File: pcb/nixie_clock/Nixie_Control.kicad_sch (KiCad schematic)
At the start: 1 part, among them U13 PCA9685BS

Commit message: nixie pin changes and more wiring
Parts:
- U28: renamed from U13; footprint Package_DFN_QFN:QFN-28-1EP_6x6mm_P0.65mm_EP4.8x4.8mm -> Package_DFN_QFN:QFN-28-1EP_6x6mm_P0.65mm_EP4.25x4.25mm
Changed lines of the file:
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@@
 		(dnp no)
 		(fields_autoplaced yes)
-		(property "Reference" "U13"
+		(property "Reference" "U28"
 			(at 96.1741 93.98 0)
 			(effects
@@
 			)
 		)
-		(property "Footprint" "Package_DFN_QFN:QFN-28-1EP_6x6mm_P0.65mm_EP4.8x4.8mm"
+		(property "Footprint" "Package_DFN_QFN:QFN-28-1EP_6x6mm_P0.65mm_EP4.25x4.25mm"
 			(at 94.615 144.145 0)
 			(effects
@@
 		(dnp no)
 		(fields_autoplaced yes)
-		(property "Reference" "#PWR014"
+		(property "Reference" "#PWR032"
 			(at 73.66 118.11 0)
 			(effects
@@
 				(path "/87768a79-2a56-4b5f-a764-e1a4021de947/d0adb527-efe9-44c8-9b93-570c1496a8be"
 					(reference "#PWR014")
+					(unit 1)
+				)
+				(path "/87768a79-2a56-4b5f-a764-e1a4021de947/e25fa4f8-0a20-4418-a3d0-fcbf589da9b2"
+					(reference "#PWR0102")
 					(unit 1)
 				)
@@
 		(dnp no)
 		(fields_autoplaced yes)
-		(property "Reference" "#PWR?"
+		(property "Reference" "#PWR034"
 			(at 93.98 92.71 0)
 			(effects
@@
 				)
 				(path "/87768a79-2a56-4b5f-a764-e1a4021de947/e25fa4f8-0a20-4418-a3d0-fcbf589da9b2"
-					(reference "#PWR?")
+					(reference "#PWR0101")
 					(unit 1)
 				)
@@
 		(dnp no)
 		(fields_autoplaced yes)
-		(property "Reference" "#PWR?"
+		(property "Reference" "#PWR033"
 			(at 91.44 161.29 0)
 			(effects
@@
 				)
 				(path "/87768a79-2a56-4b5f-a764-e1a4021de947/e25fa4f8-0a20-4418-a3d0-fcbf589da9b2"
-					(reference "#PWR?")
-					(unit 1)
-				)
+					(reference "#PWR0103")
+					(unit 1)
+				)

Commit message: remove busses and output stuff
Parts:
- renumbered U28 to U13
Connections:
- net Address0 renamed A0
- net Address1 renamed A1
- net Address2 renamed A2
- net Address3 renamed A3
- net Address4 renamed A4
- net Address5 renamed A5
- net Out_En renamed Ext_Clk

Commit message: schematic finalisation, footprint assignment and start on placeing components in layout.
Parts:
- renumbered U13 to U41
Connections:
- net Nixie_Block/Cath_0 renamed Nixie_Block2/Cath_0
- net Nixie_Block/Cath_1 renamed Nixie_Block2/Cath_1
- net Nixie_Block/Cath_2 renamed Nixie_Block2/Cath_2
- net Nixie_Block/Cath_3 renamed Nixie_Block2/Cath_3
- net Nixie_Block/Cath_4 renamed Nixie_Block2/Cath_4
- net Nixie_Block/Cath_5 renamed Nixie_Block2/Cath_5
- net Nixie_Block/Cath_6 renamed Nixie_Block2/Cath_6
- net Nixie_Block/Cath_7 renamed Nixie_Block2/Cath_7
- net Nixie_Block/Cath_8 renamed Nixie_Block2/Cath_8
- net Nixie_Block/Cath_9 renamed Nixie_Block2/Cath_9
- net Nixie_Block/Comma_L renamed Nixie_Block2/Comma_L
- net Nixie_Block/Comma_R renamed Nixie_Block2/Comma_R
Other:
- removed sheet Nixie_Block
- added sheet Nixie_Block2 (Nixie_Block.kicad_sch)
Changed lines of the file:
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@@
 		(dnp no)
 		(fields_autoplaced yes)
-		(property "Reference" "U13"
+		(property "Reference" "U41"
 			(at 96.1741 93.98 0)
 			(effects
@@
 		(dnp no)
 		(fields_autoplaced yes)
-		(property "Reference" "#PWR0102"
+		(property "Reference" "#PWR048"
 			(at 73.66 118.11 0)
 			(effects
@@
 		(dnp no)
 		(fields_autoplaced yes)
-		(property "Reference" "#PWR0101"
+		(property "Reference" "#PWR050"
 			(at 93.98 92.71 0)
 			(effects
@@
 		(dnp no)
 		(fields_autoplaced yes)
-		(property "Reference" "#PWR0103"
+		(property "Reference" "#PWR049"
 			(at 91.44 161.29 0)
 			(effects
@@
 			(color 0 0 0 0.0000)
 		)
-		(property "Sheetname" "Nixie_Block"
+		(property "Sheetname" "Nixie_Block2"
 			(at 132.08 56.4384 0)
 			(effects

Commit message: 3d models done
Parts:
- U41: LCSC Part # (none) -> C5191634
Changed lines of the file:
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@@
+			)
+		)
+		(property "LCSC Part #" "C5191634"
+			(at 93.98 119.38 0)
+			(effects
+				(font
+					(size 1.27 1.27)
+				)
+				(hide yes)
 			)
 		)

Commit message: final commits before sending to jlc
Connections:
- net +5V renamed +3V3
- net Ext_Clk renamed Out_En
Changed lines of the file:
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@@
 		)
 	)
-	(hierarchical_label "Ext_Clk"
+	(hierarchical_label "Out_En"
 		(shape input)
 		(at 46.99 109.22 180)
@@
 			)
 		)
-		(property "Value" "+5V"
+		(property "Value" "+3V3"
 			(at 93.98 83.82 0)
 			(effects

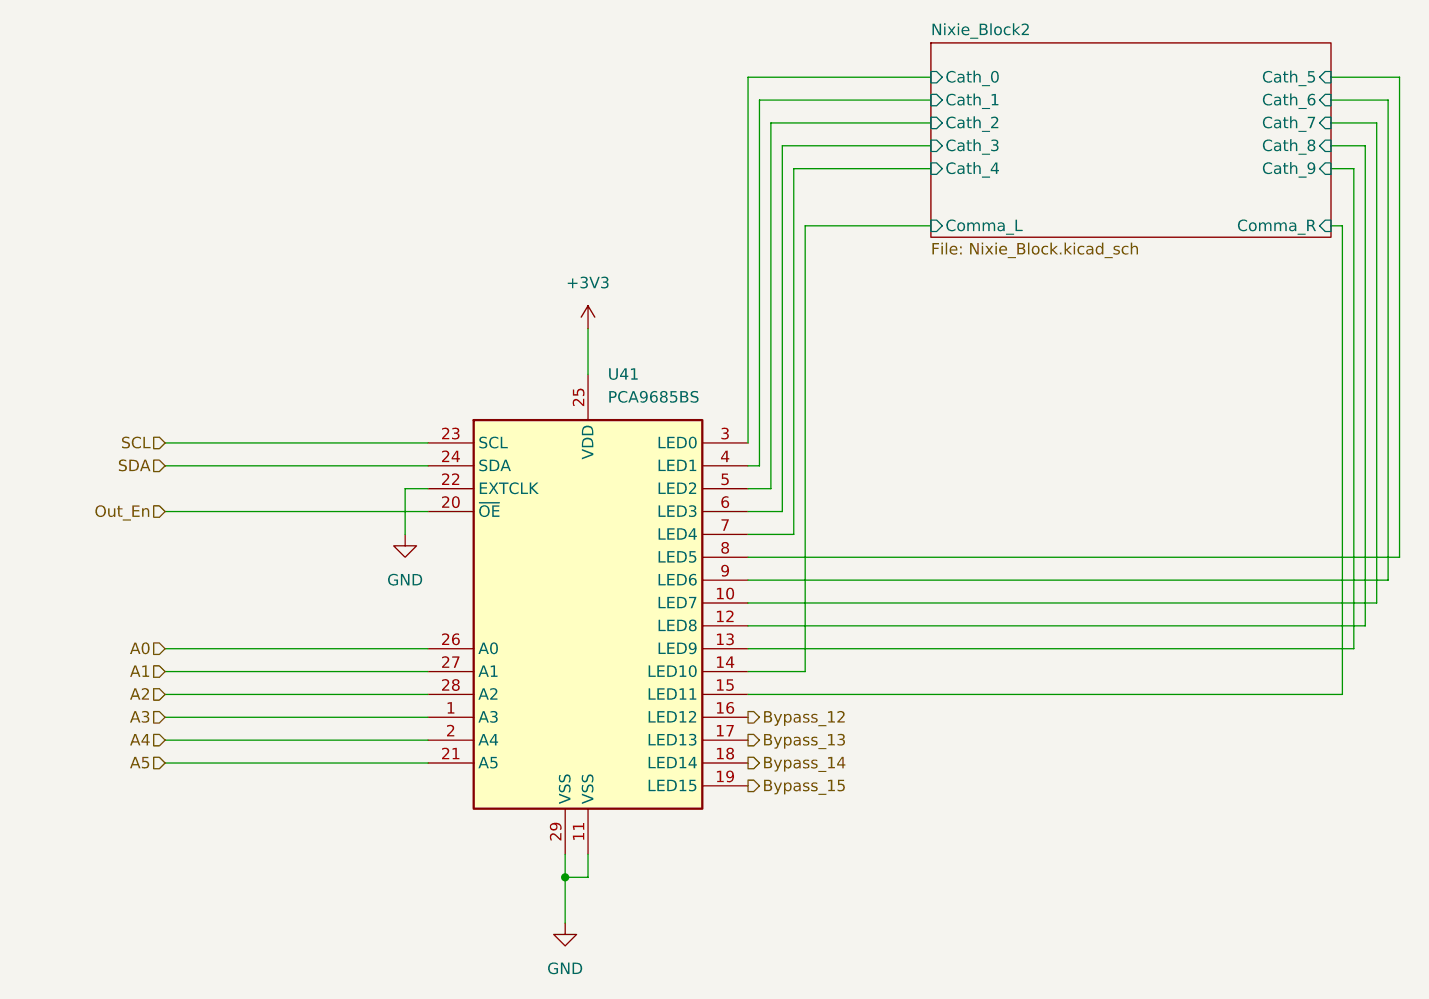
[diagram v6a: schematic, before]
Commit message: pcb changes and breakages need to fix later
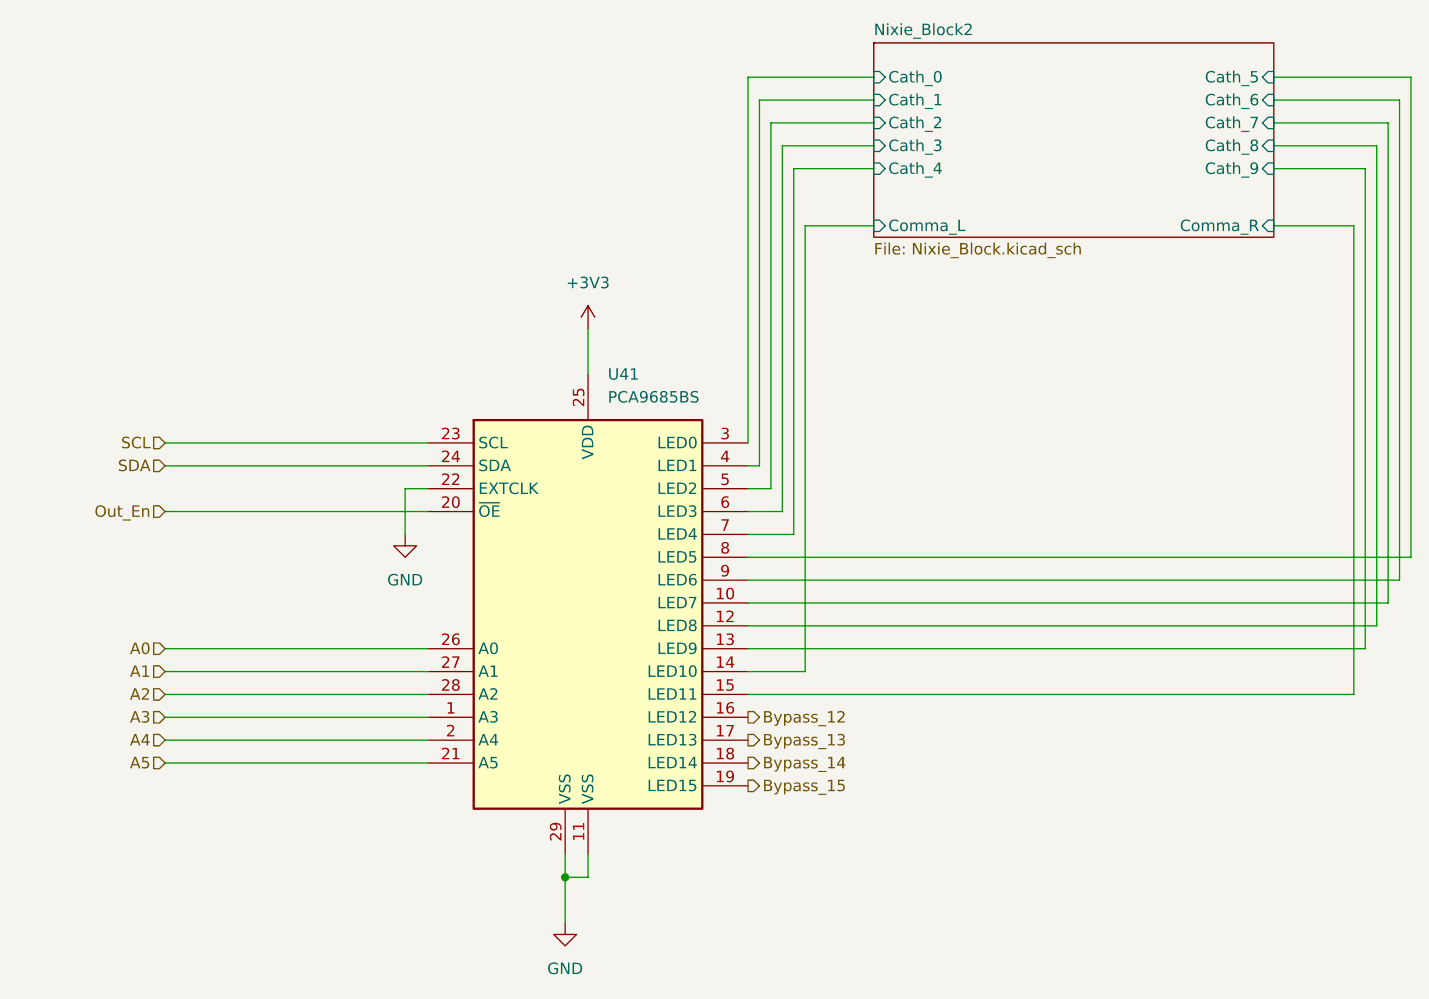
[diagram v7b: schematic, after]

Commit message: updated to kicad9
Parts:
- renumbered U41 to U13
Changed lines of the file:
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@@
 (kicad_sch
-	(version 20231120)
+	(version 20250114)
 	(generator "eeschema")
-	(generator_version "8.0")
+	(generator_version "9.0")
 	(paper "A4")
 	(junction
@@
 		(shape input)
 		(at 46.99 134.62 180)
-		(fields_autoplaced yes)
 		(effects
 			(font
@@
 		(shape input)
 		(at 46.99 101.6 180)
-		(fields_autoplaced yes)
 		(effects
 			(font
@@
 		(shape input)
 		(at 46.99 104.14 180)
-		(fields_autoplaced yes)
 		(effects
 			(font
@@
 		(shape input)
 		(at 46.99 127 180)
-		(fields_autoplaced yes)
 		(effects
 			(font
@@
 		(shape input)
 		(at 46.99 124.46 180)
-		(fields_autoplaced yes)
 		(effects
 			(font
@@
 		(shape input)
 		(at 46.99 129.54 180)
-		(fields_autoplaced yes)
 		(effects
 			(font
@@
 		(shape output)
 		(at 111.76 134.62 0)
-		(fields_autoplaced yes)
 		(effects
 			(font
@@
 		(shape output)
 		(at 111.76 139.7 0)
-		(fields_autoplaced yes)
 		(effects
 			(font
@@
 		(shape input)
 		(at 46.99 132.08 180)
-		(fields_autoplaced yes)
 		(effects
 			(font
@@
 		(shape output)
 		(at 111.76 132.08 0)
-		(fields_autoplaced yes)
 		(effects
 			(font
@@
 		(shape input)
 		(at 46.99 109.22 180)
-		(fields_autoplaced yes)
 		(effects
 			(font
@@
 		(shape input)
 		(at 46.99 137.16 180)
-		(fields_autoplaced yes)
 		(effects
 			(font
@@
 		(shape output)
 		(at 111.76 137.16 0)
-		(fields_autoplaced yes)
 		(effects
 			(font
@@
 		(dnp no)
 		(fields_autoplaced yes)
-		(property "Reference" "U41"
+		(property "Reference" "U13"
 			(at 96.1741 93.98 0)
 			(effects
@@
 		(dnp no)
 		(fields_autoplaced yes)
-		(property "Reference" "#PWR048"
+		(property "Reference" "#PWR0102"
 			(at 73.66 118.11 0)
 			(effects
@@
 		(dnp no)
 		(fields_autoplaced yes)
-		(property "Reference" "#PWR050"
+		(property "Reference" "#PWR0101"
 			(at 93.98 92.71 0)
 			(effects
@@
 		(dnp no)
 		(fields_autoplaced yes)
-		(property "Reference" "#PWR049"
+		(property "Reference" "#PWR0103"
 			(at 91.44 161.29 0)
 			(effects
@@
 		(at 125.73 57.15)
 		(size 44.45 21.59)
+		(exclude_from_sim no)
+		(in_bom yes)
+		(on_board yes)
+		(dnp no)
 		(fields_autoplaced yes)
 		(stroke
@@
 		)
 	)
+	(embedded_fonts no)
 )
